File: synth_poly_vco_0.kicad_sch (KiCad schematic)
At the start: 37 parts, among them J1 cv_in, J2 out, J3 Power, Q1 BC558, Q2 BC548, U1 40106, U2 TL074, U3 TL074, U4 TL074, U5 TL074

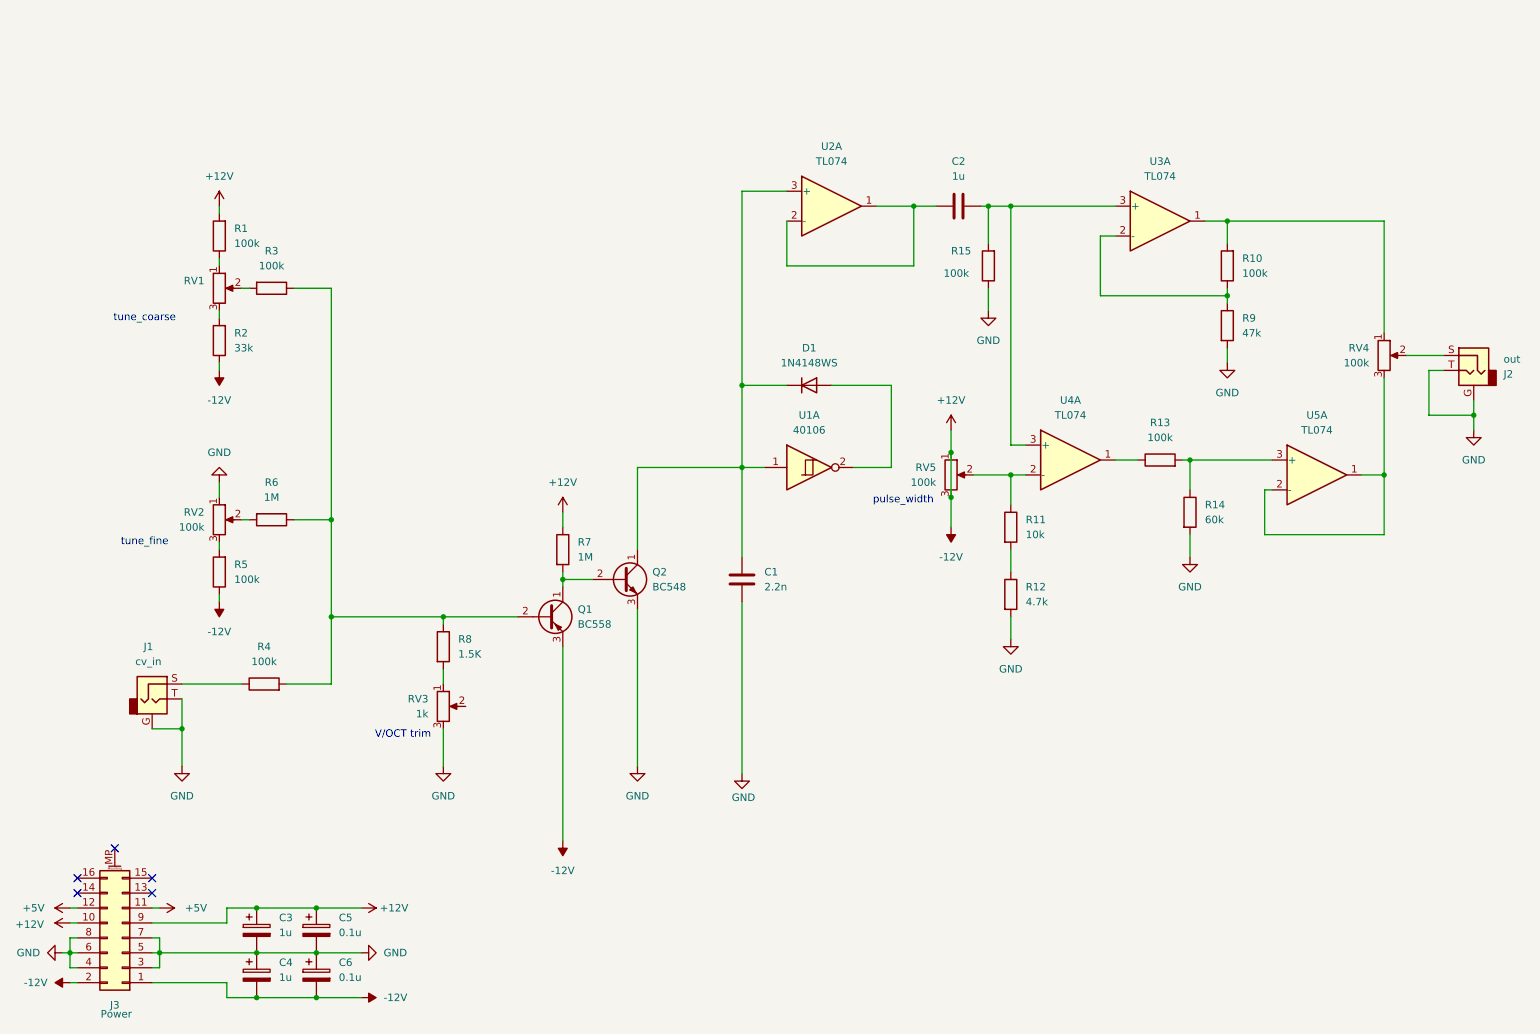
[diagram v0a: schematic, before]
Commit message: update TL074 and ST power supply
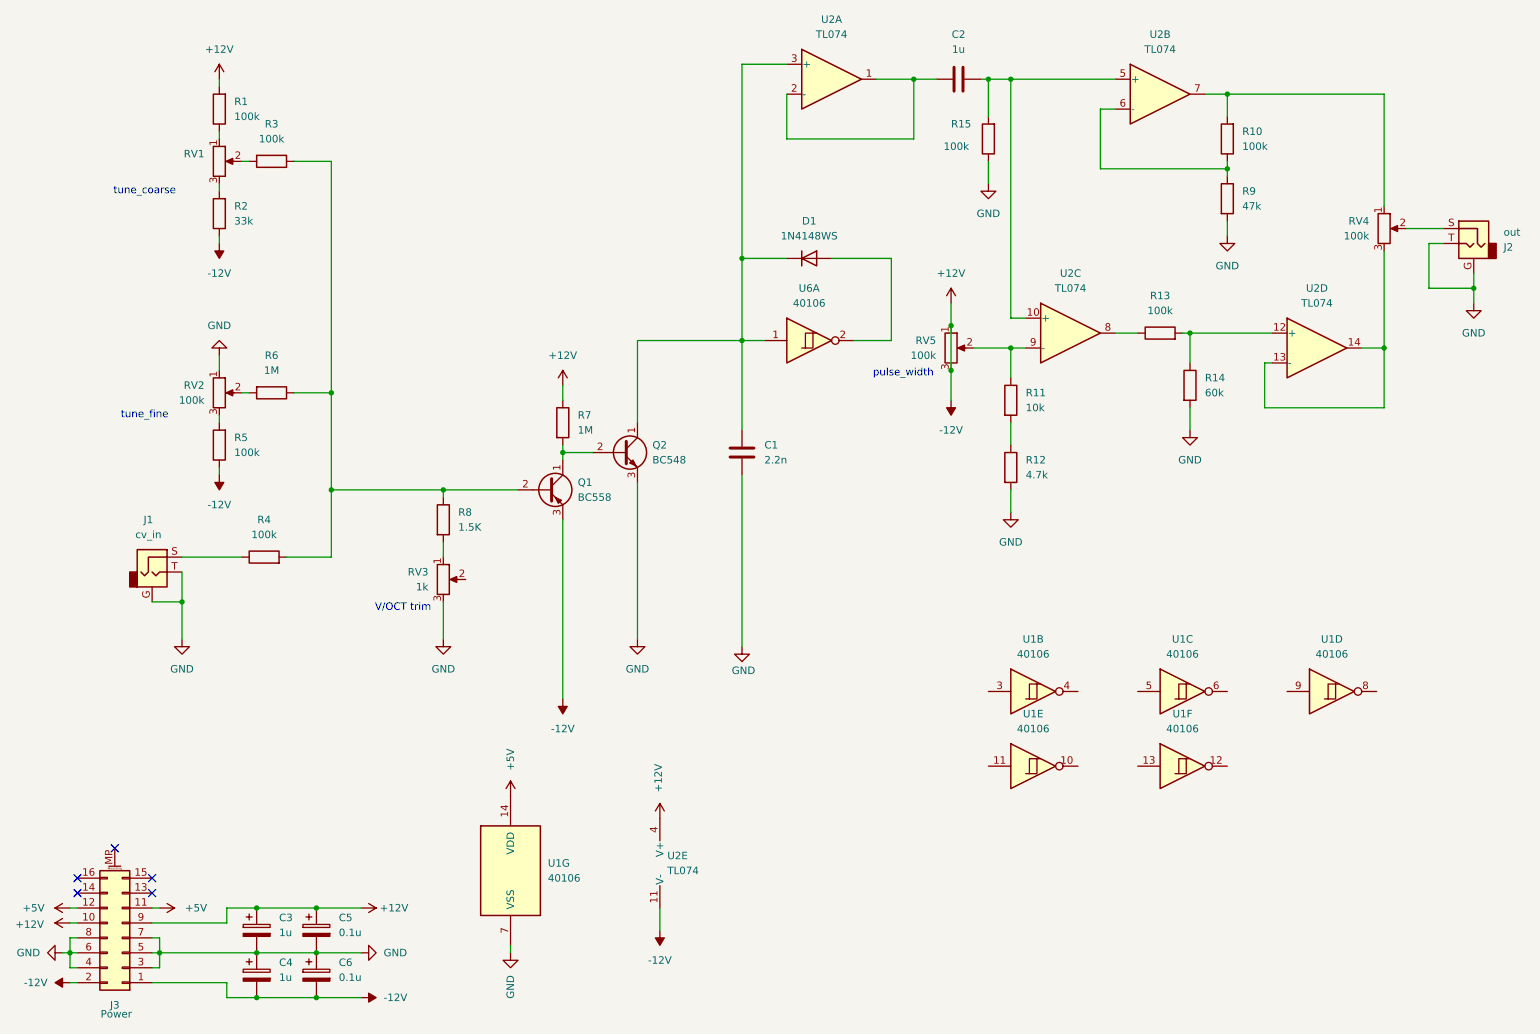
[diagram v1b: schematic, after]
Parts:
- removed U1: 40106, symbol 4xxx:40106
- removed U2, U3, U4, U5: TL074, symbol Amplifier_Operational:TL074
- added U1, U6: 40106, symbol 4xxx:40106
- added U2: TL074, symbol Amplifier_Operational:TL074
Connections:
- net +12V: now also U2.11 (V-), U2.4 (V+)
- net +5V: now also U1.14 (VDD)
- net GND: now also U1.7 (VSS)
- net at C1.1, D1.1 (K), Q2.1 (C): now also U2.3 (+), U6.1
- net at D1.2 (A): now also U6.2
- net at R13.1: now also U2.8
- net at R11.1, RV5.2: now also U2.9 (-)
- net at C2.2, R15.2: now also U2.10 (+), U2.5 (+)
- net at R10.1, R9.1: now also U2.6 (-)
- net at R10.2, RV4.1: now also U2.7
- net at C2.1: now also U2.1, U2.2 (-)
- net at RV4.3: now also U2.13 (-), U2.14
- net at R13.2, R14.1: now also U2.12 (+)
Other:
- moved on the sheet: C1, C2, D1, J1, J2, Q1, Q2, R1, R10, R11, R12, R13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

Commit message: update power flags
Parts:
- removed RV4: 100k, symbol Device:R_Potentiometer
- removed U6: 40106, symbol 4xxx:40106
- added J4: out_saw, symbol Connector_Audio:AudioJack2_Ground
- added unit 1 of U1
- added unit 3 of U2
- added unit 2 of U2
- added unit 1 of U2
- added unit 4 of U2
- J2: value out -> out_pulse
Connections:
- net GND: now also RV3.2, U1.11, U1.13, U1.3, U1.5, U1.9, J4.G, J4.T; no longer RV3.3
- net at R10.1, R9.1: now also U2.6 (-); no longer U2.6 (-)
- net at R10.2: now also J4.S, U2.7; no longer U2.7
- net at C1.1, D1.1 (K), Q2.1 (C): now also U1.1, U2.3 (+); no longer U2.3 (+)
- net at D1.2 (A): now also U1.2
- net at C2.2, R15.2: now also U2.10 (+), U2.5 (+); no longer U2.10 (+), U2.5 (+)
- net at R13.2, R14.1: now also U2.12 (+); no longer U2.12 (+)
- net at R13.1: now also U2.8; no longer U2.8
- net at R11.1, RV5.2: now also U2.9 (-); no longer U2.9 (-)
- net at J2.S: now also U2.13 (-), U2.14
- new net: C2.1, U2.1, U2.2 (-)
- no-connect marks 5 -> 11
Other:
- moved on the sheet: C3, C4, C5, C6, J2, J3, RV3, U1B, U1C, U1D, U1E, U1F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

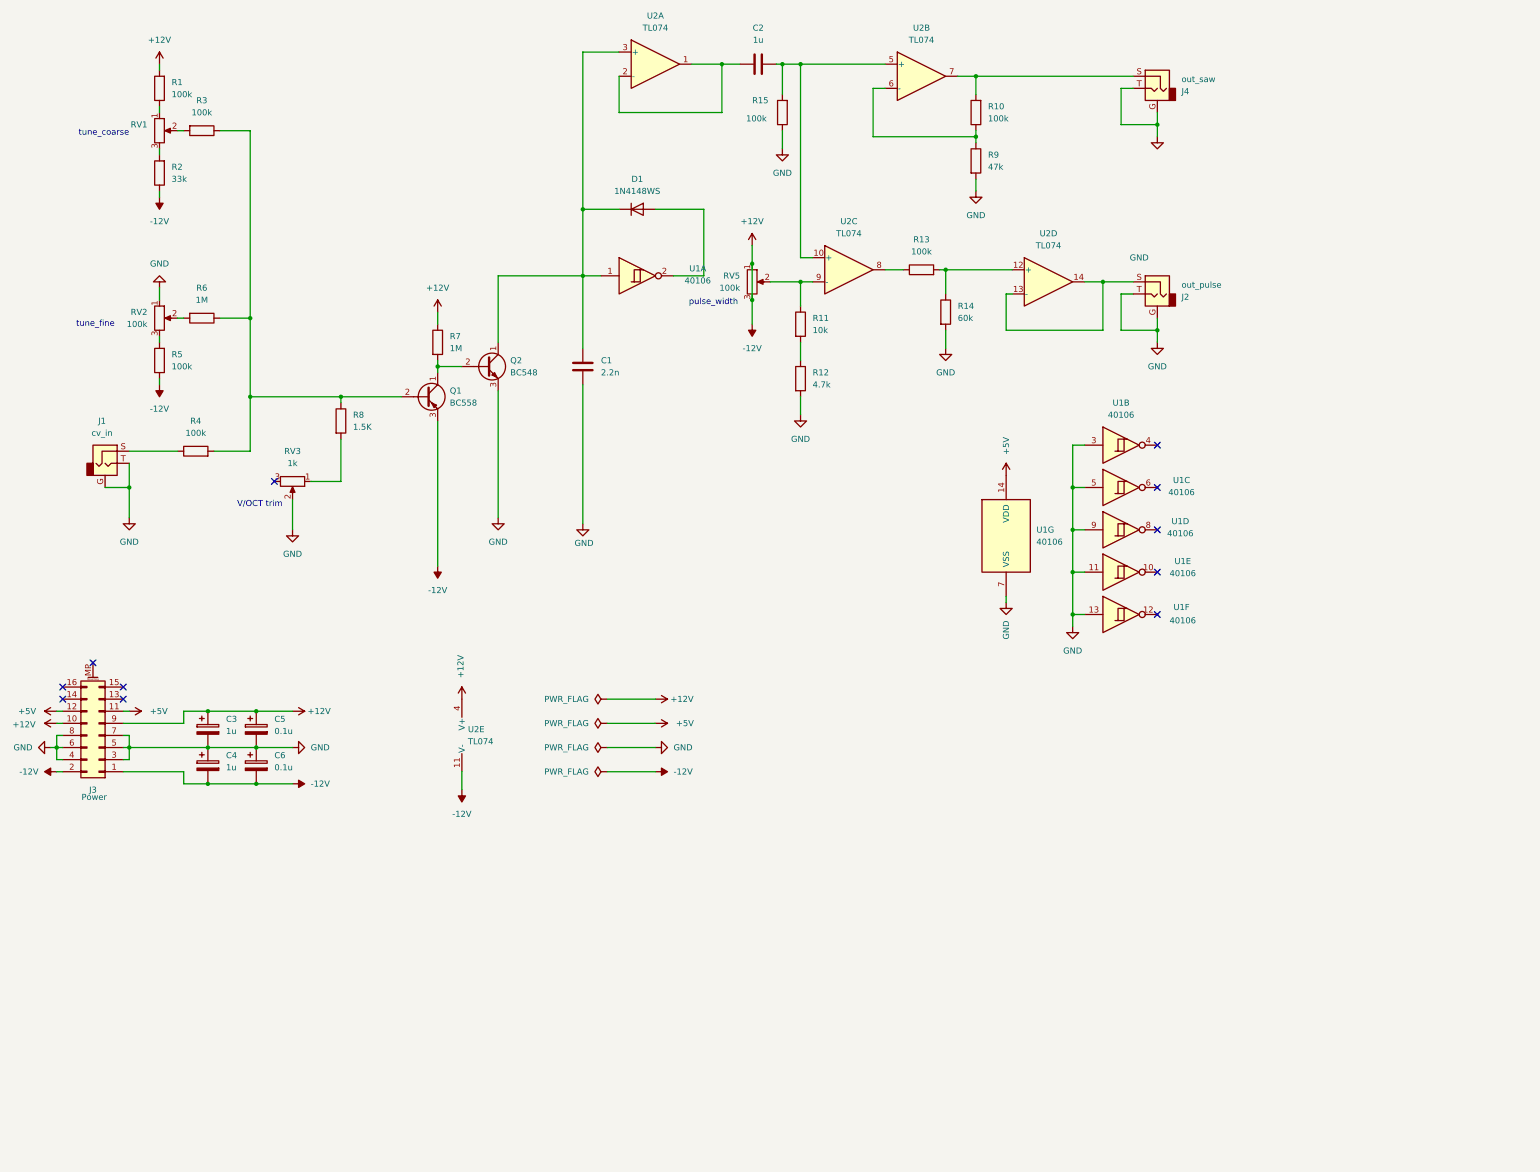
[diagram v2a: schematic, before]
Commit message: add triangle output
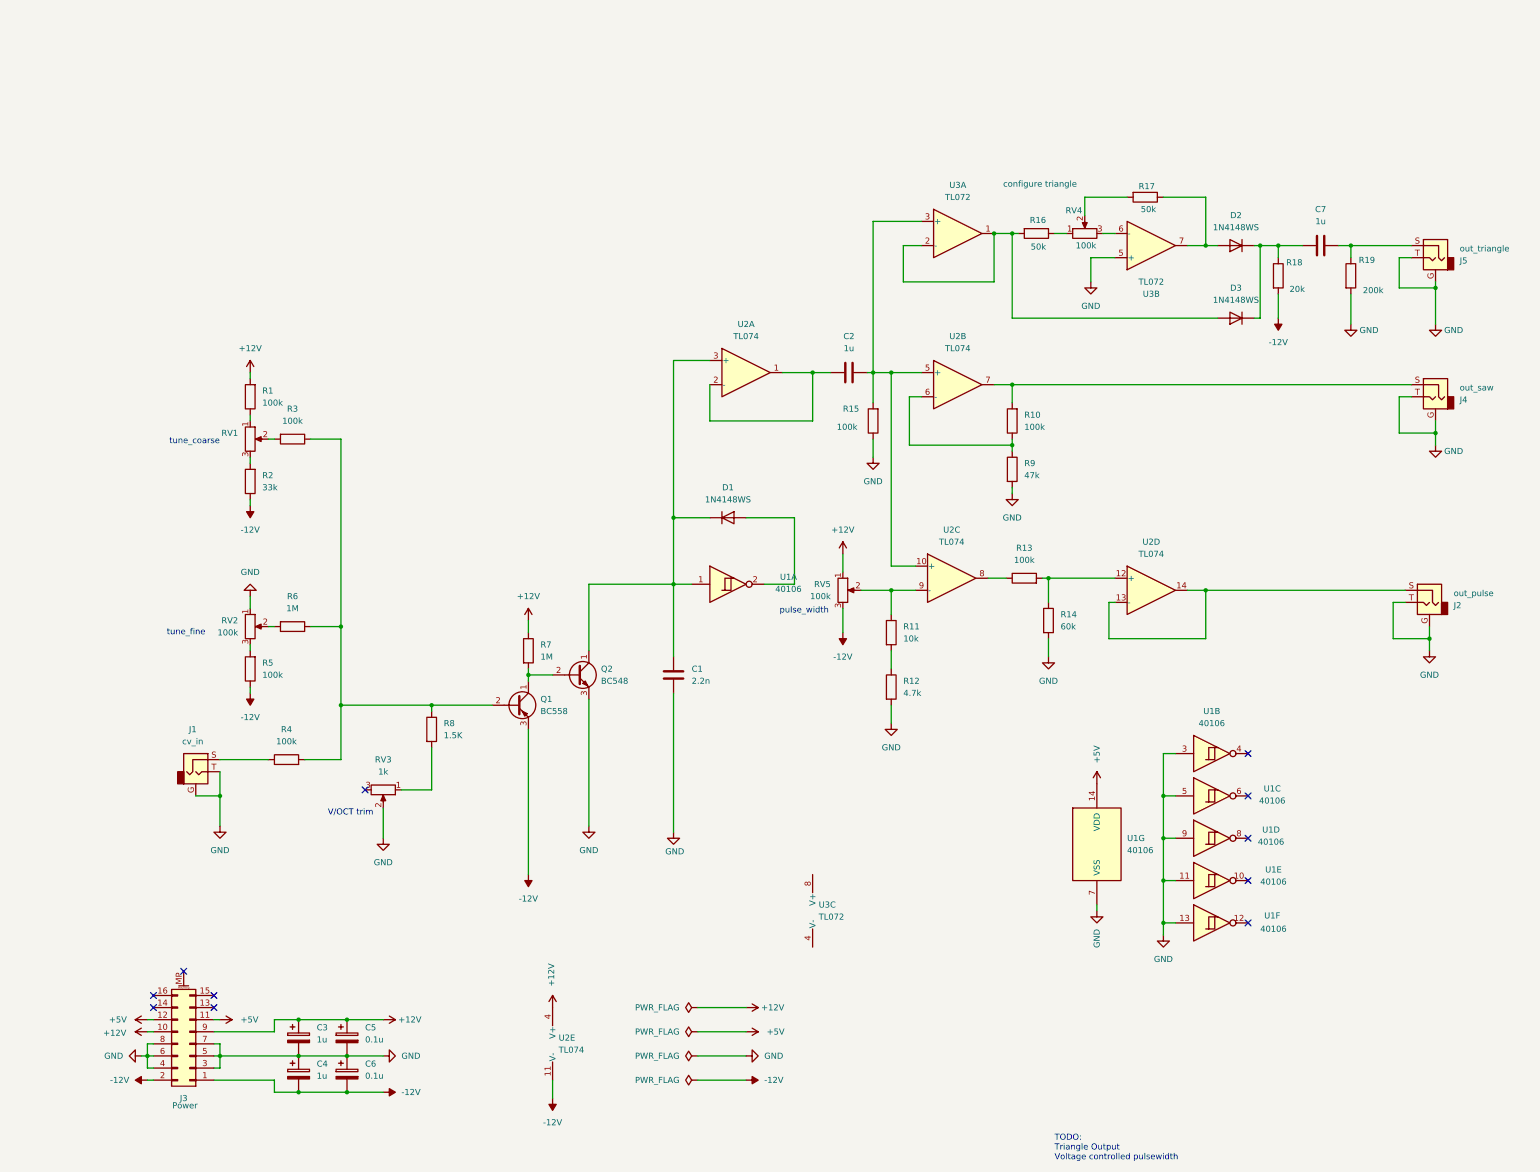
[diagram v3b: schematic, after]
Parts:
- added C7: 1u, symbol Device:C
- added D2, D3: 1N4148WS, Diode_SMD:D_SOD-323, symbol Diode:1N4148WS
- added J5: out_triangle, symbol Connector_Audio:AudioJack2_Ground
- added R16, R17: 50k, symbol Device:R
- added R18: 20k, symbol Device:R
- added R19: 200k, symbol Device:R
- added RV4: 100k, symbol Device:R_Potentiometer
- added U3: TL072, symbol Amplifier_Operational:TL072
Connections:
- net +12V: no longer C4.2, C6.2, J3.1 (Pin_1), J3.2 (Pin_2), Q1.3 (E), R2.1, R5.1, RV5.3, U2.11 (V-)
- net GND: now also J5.G, J5.T, R19.2, U3.5 (+)
- net at C2.2, R15.2, U2.10 (+)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: now also U3.3 (+)
- new net: C7.1, D2.1 (K), D3.1 (K), R18.1
- new net: D2.2 (A), R17.1, U3.7
- new net: C7.2, J5.S, R19.1
- new net: R17.2, RV4.2
- new net: D3.2 (A), R16.2, U3.1, U3.2 (-)
- new net: RV4.3, U3.6 (-)
- new net: R16.1, RV4.1
- new net -12V: C4.2, C6.2, J3.1 (Pin_1), J3.2 (Pin_2), Q1.3 (E), R18.2, R2.1, R5.1, RV5.3, U2.11 (V-)
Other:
- note added: "TODO: Triangle Output Voltage controlled pulsewidth"
- moved on the sheet: C1, C2, C3, C4, C5, C6, D1, J1, J2, J3, J4, Q1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
